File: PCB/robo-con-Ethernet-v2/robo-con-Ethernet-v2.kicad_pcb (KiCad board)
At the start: 4 copper layers, 86 x 67 mm, 98 parts, among them J1 Conn_01x04, J2 Conn_01x04, J4 RJ45_Bel_SI-60062-F, J5 Conn_01x02, J7 Conn_01x06, J8 Conn_01x06, SW1 SW_Push, SW2 SW_Push, U1 STM32G474RCTx, U10 MCP73831-2-OT, U11 LM66100DCK, U15 LM66100DCK, U18 USB_Type-C, U3 W5500, U5 RKJXV122400R, U6 NJM2884U1-33, U7 RKJXV122400R, U8 TMHU28, U9 TMHU28, Y2 XRCGB25M000FFS1AR0

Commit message: ioc と 基板やった
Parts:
- added G***: LOGO, LOGO, F.Cu at (182.1, 52.8)
- added G***: LOGO, LOGO, F.Cu at (193.0, 55.3)
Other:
- board text added: "robo-con-Ethernet-v2"

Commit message: update pcb
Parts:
- removed J7, J8: Conn_01x06, Connector_JST:JST_ZH_B6B-ZR_1x06_P1.50mm_Vertical
- removed R5: MNR04M0ABJ103, My_Library:MNR04M0ABJ103
- removed U8, U9: TMHU28, My_Library:TMHU28
- added D16: G, LED_SMD:LED_0603_1608Metric_Pad1.05x0.95mm_HandSolder, F.Cu at (116.6, 52.9)
- added D17: R, LED_SMD:LED_0603_1608Metric_Pad1.05x0.95mm_HandSolder, F.Cu at (116.6, 55.5)
- added J3: Conn_01x05, Connector_JST:JST_ZH_B5B-ZR_1x05_P1.50mm_Vertical, F.Cu at (205.3, 63.9)
- added R12: 1k, Resistor_SMD:R_0402_1005Metric_Pad0.72x0.64mm_HandSolder, F.Cu at (121.6, 34.5)
- added R13: 1k, Resistor_SMD:R_0402_1005Metric_Pad0.72x0.64mm_HandSolder, F.Cu at (121.6, 36.5)
- added R14: 1k, Resistor_SMD:R_0402_1005Metric_Pad0.72x0.64mm_HandSolder, F.Cu at (121.6, 38.5)
- added R35: 1k, Resistor_SMD:R_0402_1005Metric_Pad0.72x0.64mm_HandSolder, F.Cu at (120.4, 52.6)
- added R36: 1k, Resistor_SMD:R_0402_1005Metric_Pad0.72x0.64mm_HandSolder, F.Cu at (120.4, 54.6)
- added SW3: SW_Push, My_Library:SKHHLPA010, F.Cu at (133.5, 24.6)
- added SW4: SW_Push, My_Library:SKHHLPA010, F.Cu at (206.5, 24.6)
- added SW5: SW_Push_SPDT, My_Library:4MS1R202M6QES, F.Cu at (188.8, 44.0)
- added SW6: SW_Push_SPDT, My_Library:8MS8P1B05VS2QES-C13, F.Cu at (153.0, 56.0)
- added SW7: SW_Push_SPDT, My_Library:8MS8P1B05VS2QES-C13, F.Cu at (187.0, 56.0)
- J1: value Conn_01x04 -> Conn_01x05; footprint Connector_PinSocket_2.54mm:PinSocket_1x04_P2.54mm_Horizontal -> Connector_JST:JST_ZH_B5B-ZR_1x05_P1.50mm_Vertical; moved to F.Cu
- R24: value 2.2k -> 4k; footprint Resistor_SMD:R_0402_1005Metric_Pad0.72x0.64mm_HandSolder -> Resistor_SMD:R_0603_1608Metric_Pad0.98x0.95mm_HandSolder
- moved C24 83.2 mm to (96.0, 67.3)
- moved C25 81.3 mm to (96.0, 69.2), turned to 0 degrees
- moved R10 79.9 mm to (107.8, 49.1), turned to 0 degrees
- moved C38 74.3 mm to (99.2, 67.3), turned to 0 degrees
- moved C46 74.1 mm to (102.5, 65.3), turned to 0 degrees
- moved C45 74.0 mm to (102.5, 63.3)
- moved C44 73.0 mm to (102.5, 61.4), turned to 0 degrees
- moved D1 72.3 mm to (103.4, 34.1), turned to 0 degrees
- moved C43 71.6 mm to (102.5, 59.4)
- moved D3 71.4 mm to (103.4, 36.7), turned to 0 degrees
- moved C47 71.2 mm to (102.5, 67.3)
- moved D5 70.6 mm to (103.4, 39.3), turned to 0 degrees
- moved C34 70.5 mm to (99.2, 59.4), turned to 0 degrees
- moved C36 70.5 mm to (99.2, 63.3), turned to 0 degrees
- moved D10 70.0 mm to (103.4, 41.9), turned to 0 degrees
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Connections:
- net VBUS renamed Net-(U11-VIN)
- J1 pad 1: GND -> +3.3V
- J1 pad 2: SWDIO -> R1_BUTTON
- J1 pad 3: SWCLK -> R2_BUTTON
- J1 pad 4: NRST -> R3_BUTTON
- R11 pad 1: ST_LED_3 -> LED3
- R2 pad 1: ST_LED_0 -> LED0
- R32 pad 1: ST_LED_4 -> LED4
- R33 pad 1: ST_LED_USB -> LEDUSB
- R34 pad 1: ST_LED_W5500 -> LEDW5500
- R4 pad 1: ST_LED_1 -> LED1
- R6 pad 1: ST_LED_2 -> LED2
- R79 pad 1: +5V -> V_ON
- R79 pad 2: Net-(U6-CONT) -> Net-(SW5-B)
- U1 pad 10: Left_Push_Stick -> unconnected-(U1-PC2-Pad10)
- U1 pad 11: Right_Push_Stick -> unconnected-(U1-PC3-Pad11)
- U1 pad 17: LiPo_Observe -> unconnected-(U1-PA3-Pad17)
- U1 pad 18: W5500_nCS -> unconnected-(U1-PA4-Pad18)
- U1 pad 19: W5500_SCLK -> unconnected-(U1-PA5-Pad19)
- U1 pad 2: ST_LED_4 -> unconnected-(U1-PC13-Pad2)
- U1 pad 20: W5500_MISO -> unconnected-(U1-PA6-Pad20)
- U1 pad 21: W5500_MOSI -> unconnected-(U1-PA7-Pad21)
- U1 pad 22: Right_Button_8 -> unconnected-(U1-PC4-Pad22)
- U1 pad 24: W5500_nINT -> unconnected-(U1-PB0-Pad24)
- U1 pad 25: W5500_nRST -> unconnected-(U1-PB1-Pad25)
- U1 pad 3: ST_LED_3 -> unconnected-(U1-PC14-Pad3)
- U1 pad 30: Wio-E5_RST -> unconnected-(U1-PB10-Pad30)
- U1 pad 33: Right_X_Stick -> unconnected-(U1-PB11-Pad33)
- U1 pad 34: Right_Y_Stick -> unconnected-(U1-PB12-Pad34)
- U1 pad 35: Right_Button_5 -> unconnected-(U1-PB13-Pad35)
- U1 pad 36: Right_Button_6 -> unconnected-(U1-PB14-Pad36)
- U1 pad 37: Right_Button_7 -> unconnected-(U1-PB15-Pad37)
- U1 pad 38: Right_Lever_Switch_2 -> unconnected-(U1-PC6-Pad38)
- U1 pad 39: Right_Lever_Switch_1 -> unconnected-(U1-PC7-Pad39)
- U1 pad 4: ST_LED_2 -> unconnected-(U1-PC15-Pad4)
- U1 pad 40: Right_Lever_Switch_0 -> unconnected-(U1-PC8-Pad40)
- U1 pad 41: Right_Lever_Switch_4 -> unconnected-(U1-PC9-Pad41)
- U1 pad 42: Right_Lever_Switch_3 -> unconnected-(U1-PA8-Pad42)
- U1 pad 43: ST_LED_W5500 -> unconnected-(U1-PA9-Pad43)
- U1 pad 44: ST_LED_USB -> unconnected-(U1-PA10-Pad44)
- U1 pad 5: ST_LED_1 -> unconnected-(U1-PF0-Pad5)
- U1 pad 51: Left_Button_1 -> unconnected-(U1-PA15-Pad51)
- U1 pad 52: Left_Button_2 -> unconnected-(U1-PC10-Pad52)
- U1 pad 53: Left_Button_3 -> unconnected-(U1-PC11-Pad53)
- U1 pad 54: Left_Button_4 -> unconnected-(U1-PC12-Pad54)
- U1 pad 56: Left_Lever_Switch_3 -> unconnected-(U1-PB3-Pad56)
- U1 pad 57: Left_Lever_Switch_4 -> unconnected-(U1-PB4-Pad57)
- U1 pad 58: Left_Lever_Switch_0 -> unconnected-(U1-PB5-Pad58)
- U1 pad 59: Left_Lever_Switch_2 -> unconnected-(U1-PB6-Pad59)
- U1 pad 6: ST_LED_0 -> unconnected-(U1-PF1-Pad6)
- U1 pad 60: Left_Lever_Switch_1 -> unconnected-(U1-PB7-Pad60)
- U1 pad 8: Left_X_Stick -> unconnected-(U1-PC0-Pad8)
- U1 pad 9: Left_Y_Stick -> unconnected-(U1-PC1-Pad9)
- U18 pad S1: GND -> unconnected-(U18-SHIELD-PadS1)
- U5 pad 2: Left_X_Stick -> LX_STICK
- U5 pad 5: Left_Y_Stick -> LY_STICK
- U5 pad b: Left_Push_Stick -> LP_STICK
- U5 pad d: Left_Push_Stick -> LP_STICK
- U6 pad 1: Net-(U6-CONT) -> V_ON
- U7 pad 2: Right_X_Stick -> RX_STICK
- U7 pad 5: Right_Y_Stick -> RY_STICK
- U7 pad b: Right_Push_Stick -> RP_STICK
- U7 pad d: Right_Push_Stick -> RP_STICK
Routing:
- net +3.3V: track 470.5 -> 2.77 mm, vias 13 -> 0
- net SWDIO: track 108.3 -> 0.00 mm, vias 2 -> 0
- net SWCLK: track 107.8 -> 0.00 mm, vias 3 -> 0
- net Right_Push_Stick: track 88.5 -> 0.00 mm, vias 2 -> 0
- net Right_Lever_Switch_3: track 81.8 -> 0.00 mm, vias 2 -> 0
- net Right_Lever_Switch_4: track 77.7 -> 0.00 mm, vias 2 -> 0
- net Right_Lever_Switch_0: track 74.7 -> 0.00 mm, vias 2 -> 0
- net Right_Lever_Switch_2: track 72.5 -> 0.00 mm, vias 2 -> 0
- net Right_Lever_Switch_1: track 72.2 -> 0.00 mm, vias 2 -> 0
- net Right_Y_Stick: track 71.5 -> 0.00 mm, vias 1 -> 0
- net +5V: track 65.5 -> 4.46 mm, vias 2 -> 0
- net Right_Button_8: track 60.2 -> 0.00 mm, vias 1 -> 0
- net GND: track 59.6 -> 0.00 mm, vias 165 -> 0
- net Right_Button_7: track 59.1 -> 0.00 mm, vias 2 -> 0
- net Right_Button_6: track 58.8 -> 0.00 mm, vias 2 -> 0
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- removed copper zone on B.Cu, net GND
- removed copper zone on F.Cu, net GND
- removed copper zone on In1.Cu, net GND
- removed copper zone on In2.Cu, net GND
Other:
- board text removed: "+3.3V"
- board text removed: "BOOT0"
- board text removed: "GND"
- board text removed: "NRST"
- board text removed: "Nromal"
- board text removed: "Original"
- board text removed: "ST_0"
- board text removed: "ST_1"
- board text removed: "ST_2"
- board text removed: "ST_3"
- board text removed: "ST_4"
- board text removed: "SWCLK"
- board text removed: "SWDIO"
- board text removed: "USB"
- board text removed: "W5500"

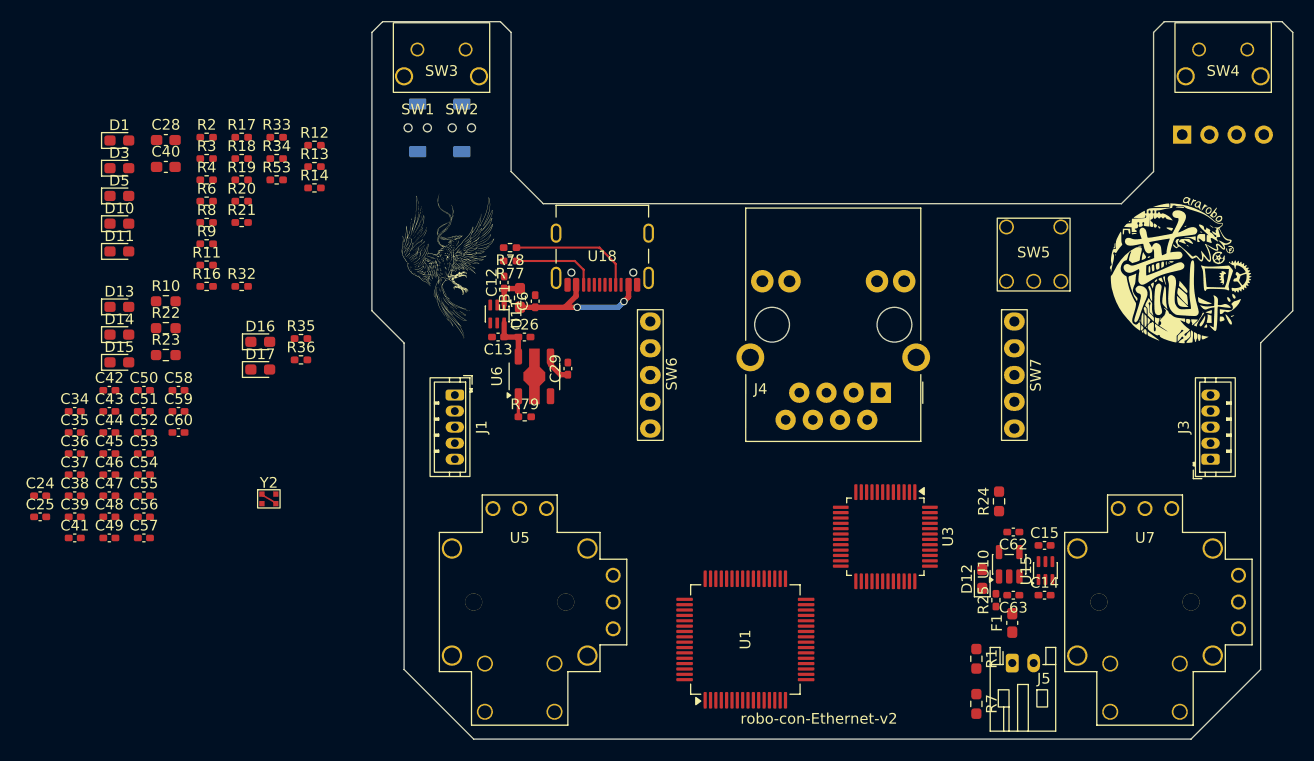
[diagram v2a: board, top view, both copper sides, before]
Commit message: PCBのGNDビア打ち以外終了 iocファイルとの照合はまだ 明日やる
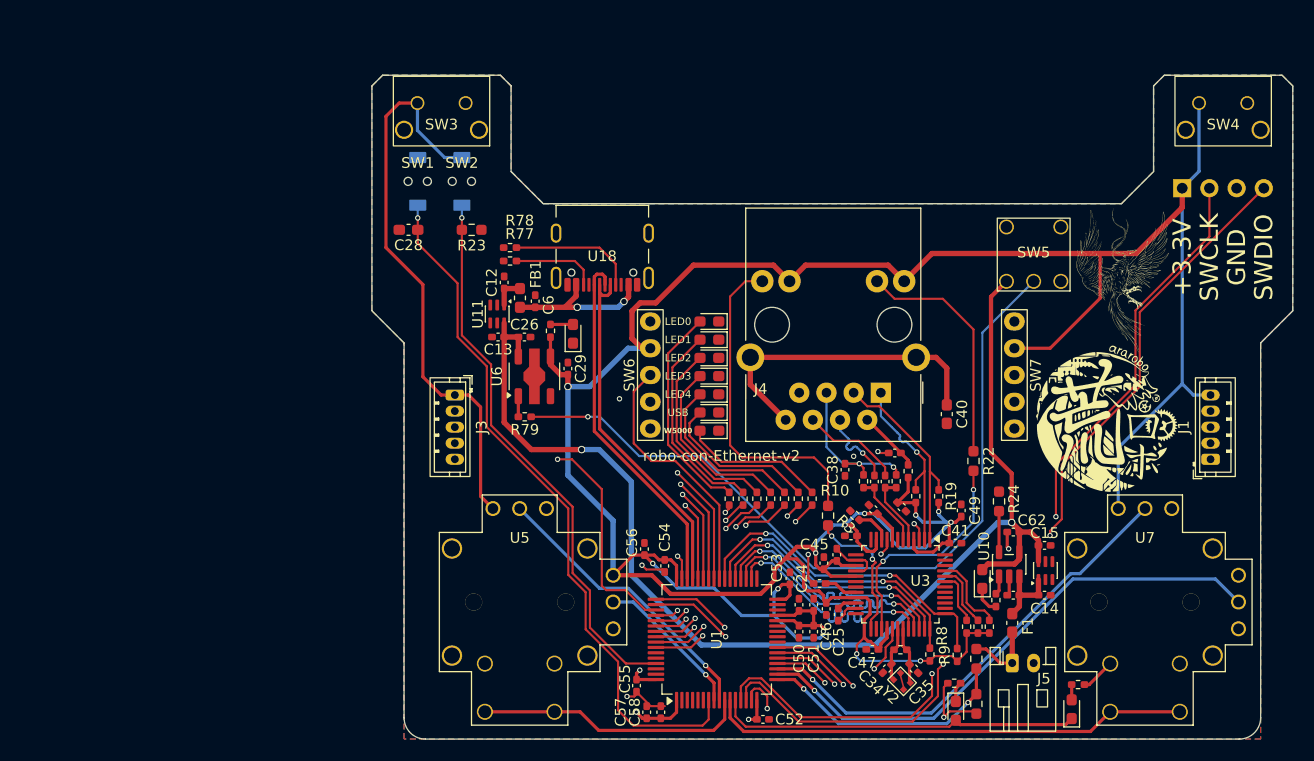
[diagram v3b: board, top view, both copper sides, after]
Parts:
- moved D16 83.2 mm to (192.4, 87.2), turned to 90 degrees
- moved C41 82.2 mm to (181.5, 71.7)
- moved C35 81.4 mm to (177.6, 83.4), turned to -45 degrees
- moved R9 79.9 mm to (181.7, 82.1), turned to 90 degrees
- moved C49 79.6 mm to (182.0, 68.7), turned to 90 degrees
- moved C34 79.6 mm to (175.1, 83.4), turned to -135 degrees
- moved R35 79.4 mm to (192.9, 84.9), turned to 180 degrees
- moved R8 78.7 mm to (179.1, 82.1), turned to 90 degrees
- moved R12 77.4 mm to (184.7, 79.5), turned to 90 degrees
- moved C39 76.8 mm to (175.8, 63.3), turned to 180 degrees
- moved C40 76.5 mm to (180.7, 59.6), turned to -90 degrees
- moved R22 76.4 mm to (183.2, 64.0), turned to -90 degrees
- moved C37 75.7 mm to (174.9, 66.0), turned to 90 degrees
- moved R13 75.4 mm to (183.6, 79.5), turned to 90 degrees
- moved C25 75.1 mm to (170.5, 78.4), turned to -90 degrees
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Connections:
- J1 pad 1: +3.3V -> R4_BUTTON
- J1 pad 2: R1_BUTTON -> R3_BUTTON
- J1 pad 4: R3_BUTTON -> R1_BUTTON
- J1 pad 5: R4_BUTTON -> +3.3V
- J3 pad 1: L8_BUTTON -> +3.3V
- J3 pad 2: L7_BUTTON -> L5_BUTTON
- J3 pad 4: L5_BUTTON -> L7_BUTTON
- J3 pad 5: +3.3V -> L8_BUTTON
- U1 pad 10: unconnected-(U1-PC2-Pad10) -> LP_STICK
- U1 pad 11: unconnected-(U1-PC3-Pad11) -> RP_STICK
- U1 pad 12: unconnected-(U1-PA0-Pad12) -> LEDLiPo
- U1 pad 13: unconnected-(U1-PA1-Pad13) -> R_PUSH_UP
- U1 pad 14: unconnected-(U1-PA2-Pad14) -> R_PUSH
- U1 pad 17: unconnected-(U1-PA3-Pad17) -> LiPo_Observe
- U1 pad 18: unconnected-(U1-PA4-Pad18) -> RY_STICK
- U1 pad 19: unconnected-(U1-PA5-Pad19) -> RX_STICK
- U1 pad 20: unconnected-(U1-PA6-Pad20) -> R4_BUTTON
- U1 pad 21: unconnected-(U1-PA7-Pad21) -> R3_BUTTON
- U1 pad 22: unconnected-(U1-PC4-Pad22) -> R2_BUTTON
- U1 pad 23: unconnected-(U1-PC5-Pad23) -> R1_BUTTON
- U1 pad 34: unconnected-(U1-PB12-Pad34) -> W5500_nCS
- U1 pad 35: unconnected-(U1-PB13-Pad35) -> W5500_SCLK
- U1 pad 36: unconnected-(U1-PB14-Pad36) -> W5500_MISO
- U1 pad 37: unconnected-(U1-PB15-Pad37) -> W5500_MOSI
- U1 pad 38: unconnected-(U1-PC6-Pad38) -> W5500_nINT
- U1 pad 39: unconnected-(U1-PC7-Pad39) -> W5500_nRST
- U1 pad 40: unconnected-(U1-PC8-Pad40) -> L_PUSH_UP
- U1 pad 41: unconnected-(U1-PC9-Pad41) -> L5_BUTTON
- U1 pad 42: unconnected-(U1-PA8-Pad42) -> L6_BUTTON
- U1 pad 43: unconnected-(U1-PA9-Pad43) -> L7_BUTTON
- U1 pad 44: unconnected-(U1-PA10-Pad44) -> L8_BUTTON
- U1 pad 51: unconnected-(U1-PA15-Pad51) -> L_PUSH
- U1 pad 52: unconnected-(U1-PC10-Pad52) -> LED0
- U1 pad 53: unconnected-(U1-PC11-Pad53) -> LED1
- U1 pad 54: unconnected-(U1-PC12-Pad54) -> LED2
- U1 pad 55: unconnected-(U1-PD2-Pad55) -> LED3
- U1 pad 56: unconnected-(U1-PB3-Pad56) -> LED4
- U1 pad 57: unconnected-(U1-PB4-Pad57) -> LEDUSB
- U1 pad 58: unconnected-(U1-PB5-Pad58) -> LEDW5500
- U1 pad 8: unconnected-(U1-PC0-Pad8) -> LY_STICK
- U1 pad 9: unconnected-(U1-PC1-Pad9) -> LX_STICK
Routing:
- net +3.3V: track 2.77 -> 484.2 mm, vias 0 -> 15
- net +5V: track 4.46 -> 113.9 mm, vias 0 -> 2
- net SWDIO: track 0.00 -> 96.6 mm, vias 0 -> 2
- net SWCLK: track 0.00 -> 94.9 mm, vias 0 -> 2
- net R_PUSH: track 0.00 -> 94.2 mm, vias 0 -> 1
- net Net-(SW5-B): track 0.00 -> 74.2 mm, vias 0 -> 1
- net NRST: track 0.00 -> 66.0 mm, vias 0 -> 1
- net L_PUSH: track 0.00 -> 58.2 mm, vias 0 -> 1
- net R1_BUTTON: track 0.00 -> 57.9 mm, vias 0 -> 1
- net R2_BUTTON: track 0.00 -> 57.4 mm, vias 0 -> 1
- net R3_BUTTON: track 0.00 -> 56.9 mm, vias 0 -> 1
- net R4_BUTTON: track 0.00 -> 56.4 mm, vias 0 -> 1
- net R_PUSH_UP: track 0.00 -> 56.0 mm, vias 0 -> 1
- net BOOT0: track 0.00 -> 52.0 mm, vias 0 -> 1
- net RY_STICK: track 0.00 -> 51.0 mm, vias 0 -> 1
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- added copper zone on B.Cu, net GND
- added copper zone on F.Cu, net GND
- added copper zone on In1.Cu, net GND
- added copper zone on In2.Cu, net GND
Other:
- board size 86 x 67 mm -> 86 x 62 mm
- board text added: "+3.3V"
- board text added: "BOOT0"
- board text added: "GND"
- board text added: "LED0"
- board text added: "LED1"
- board text added: "LED2"
- board text added: "LED3"
- board text added: "LED4"
- board text added: "NRST"
- board text added: "SWCLK"
- board text added: "SWDIO"
- board text added: "USB"
- board text added: "W5000"

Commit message: ioc 比較済み
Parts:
- added REF**: MountingHole_2.2mm_M2, MountingHole:MountingHole_2.2mm_M2, F.Cu at (207.0, 87.0)
- added REF**: MountingHole_2.2mm_M2, MountingHole:MountingHole_2.2mm_M2, F.Cu at (133.0, 87.0)
- added REF**: MountingHole_2.2mm_M2, MountingHole:MountingHole_2.2mm_M2, F.Cu at (207.0, 53.0)
- added REF**: MountingHole_2.2mm_M2, MountingHole:MountingHole_2.2mm_M2, F.Cu at (133.0, 53.0)
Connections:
- net L_PUSH_UP renamed L_PUSH_HOME
- net R_PUSH_UP renamed R_PUSH_HOME
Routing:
- net +3.3V: track 484.2 -> 485.6 mm
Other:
- board text added: "BAD"
- board text added: "C3"
- board text added: "GOOD"
- board text added: "LiPo"
- board text added: "R2"
- board text added: "外径左右対称"
- board text added: "指定なしはC1"

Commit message: v2 PCB ガーバー
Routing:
- net SWCLK: track 94.9 -> 96.5 mm
- net GND: vias 13 -> 40

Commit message: up
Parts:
- moved D11 15.8 mm to (158.3, 42.5), turned to -90 degrees
- moved R21 15.3 mm to (156.8, 44.0)
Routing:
- net +3.3V: track 485.6 -> 485.0 mm
- net Net-(D11-A): track 2.10 -> 1.55 mm
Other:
- board text added: "POWER"
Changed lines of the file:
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@@
 	(footprint "LED_SMD:LED_0603_1608Metric_Pad1.05x0.95mm_HandSolder"
 		(layer "F.Cu")
-		(at 145.78 52.149999 90)
+		(at 158.35 42.525001 -90)
 		(descr "LED SMD 0603 (1608 Metric), square (rectangular) end terminal, IPC-7351 nominal, (Body size source: http://www.tortai-tech.com/upload/download/2011102023233369053.pdf)")
 		(tags "LED handsolder")
 		(property "Reference" "D11"
-			(at -0.000001 0 270)
+			(at -0.000001 0 90)
 			(layer "B.SilkS")
 			(effects
@@
 		)
 		(property "Sim.Pins" "1=K 2=A"
-			(at 0 0 90)
+			(at 0 0 270)
 			(unlocked yes)
 			(layer "F.Fab")
@@
 		(duplicate_pad_numbers_are_jumpers no)
 		(fp_line
-			(start 0.8 -0.735)
-			(end -1.66 -0.735)
+			(start -1.66 0.735)
+			(end 0.8 0.735)
 			(stroke
 				(width 0.12)
@@
 		)
 		(fp_line
-			(start -1.66 0.735)
-			(end 0.8 0.735)
+			(start 0.8 -0.735)
+			(end -1.66 -0.735)
 			(stroke
 				(width 0.12)
@@
 		)
 		(fp_line
-			(start 0.8 -0.4)
-			(end -0.5 -0.4)
+			(start -0.8 0.4)
+			(end 0.8 0.4)
 			(stroke
 				(width 0.1)
@@
 		)
 		(fp_line
-			(start -0.5 -0.4)
-			(end -0.8 -0.1)
+			(start 0.8 0.4)
+			(end 0.8 -0.4)
 			(stroke
 				(width 0.1)
@@
 		)
 		(fp_line
-			(start 0.8 0.4)
-			(end 0.8 -0.4)
+			(start -0.5 -0.4)
+			(end -0.8 -0.1)
 			(stroke
 				(width 0.1)
@@
 		)
 		(fp_line
-			(start -0.8 0.4)
-			(end 0.8 0.4)
+			(start 0.8 -0.4)
+			(end -0.5 -0.4)
 			(stroke
 				(width 0.1)
@@
 		)
 		(pad "1" smd roundrect
-			(at -0.874999 0 90)
+			(at -0.874999 0 270)
 			(size 1.05 0.95)
 			(layers "F.Cu" "F.Mask" "F.Paste")
@@
 		)
 		(pad "2" smd roundrect
-			(at 0.874999 0 90)
+			(at 0.874999 0 270)
 			(size 1.05 0.95)
 			(layers "F.Cu" "F.Mask" "F.Paste")
@@
 	(footprint "Resistor_SMD:R_0402_1005Metric_Pad0.72x0.64mm_HandSolder"
 		(layer "F.Cu")
-		(at 143.675 51.8725 90)
+		(at 156.8 43.9975 90)
 		(descr "Resistor SMD 0402 (1005 Metric), square (rectangular) end terminal, IPC-7351 nominal with elongated pad for handsoldering. (Body size source: IPC-SM-782 page 72, https://www.pcb-3d.com/wordpress/wp-content/uploads/ipc-sm-782a_amendment_1_and_2.pdf)")
 		(tags "resistor handsolder")
@@
 		)
 	)
+	(gr_text "+3.3V"
+		(at 159.85 42.75 90)
+		(layer "F.SilkS")
+		(effects
+			(font
+				(size 0.7 0.7)
+				(thickness 0.15)
+			)
+		)
+	)
 	(gr_text "BAD"
 		(at 179.7 87.29 90)
@@
 		)
 	)
+	(gr_text "POWER"
+		(at 182.9 46.8 90)
+		(layer "F.SilkS")
+		(effects
+			(font
+				(size 1.7 1.7)
+				(thickness 0.25)
+			)
+		)
+	)
 	(gr_text "+3.3V"
 		(at 202.675 45.000001 90)
@@
 	)
 	(segment
-		(start 143.675 52.47)
-		(end 143.675 54.275)
-		(width 0.3)
-		(layer "F.Cu")
-		(net "+3.3V")
-	)
-	(segment
 		(start 138.3 68.47)
 		(end 137.15 67.32)
@@
 	)
 	(segment
+		(start 156.8 45.509998)
+		(end 157.030001 45.739999)
+		(width 0.2)
+		(layer "F.Cu")
+		(net "+3.3V")
+	)
+	(segment
 		(start 168.255 79.4)
 		(end 166.885 79.4)
@@
 	)
 	(segment
+		(start 156.8 44.595)
+		(end 156.8 45.509998)
+		(width 0.2)
+		(layer "F.Cu")
+		(net "+3.3V")
+	)
+	(segment
 		(start 153.8125 73.2625)
 		(end 154.345 73.2625)
@@
 	)
 	(segment
-		(start 143.675 51.275)
-		(end 145.78 51.275)
-		(width 0.3)
+		(start 156.8 43.4)
+		(end 158.35 43.4)
+		(width 0.2)
 		(layer "F.Cu")
 		(net "Net-(D11-A)")
